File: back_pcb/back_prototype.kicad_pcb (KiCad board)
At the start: 2 copper layers, 40 x 100 mm, 358 parts

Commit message: Started new back PCB
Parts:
- removed ? (x330): , single_proto_pad:PROTO_PAD
- removed AB2_PERF_RAILS_1x1.7IN: VAL**, prototyping_area_10x14:PROTO_AREA_10x14
- removed W10: RXD, Measurement_Points:Measurement_Point_Square-SMD-Pad_Small
- removed W13: SDA, Measurement_Points:Measurement_Point_Square-SMD-Pad_Small
- removed W14: SCL, Measurement_Points:Measurement_Point_Square-SMD-Pad_Small
- removed W15: MOSI, Measurement_Points:Measurement_Point_Square-SMD-Pad_Small
- removed W16: MISO, Measurement_Points:Measurement_Point_Square-SMD-Pad_Small
- removed W17: SCK, Measurement_Points:Measurement_Point_Square-SMD-Pad_Small
- removed W18: , Measurement_Points:Measurement_Point_Square-SMD-Pad_Small
- removed W19: CS1, Measurement_Points:Measurement_Point_Square-SMD-Pad_Small
- removed W20: GP4, Measurement_Points:Measurement_Point_Square-SMD-Pad_Small
- removed W21: GP17, Measurement_Points:Measurement_Point_Square-SMD-Pad_Small
- removed W22: GP12, Measurement_Points:Measurement_Point_Square-SMD-Pad_Small
- removed W23: GP16, Measurement_Points:Measurement_Point_Square-SMD-Pad_Small
- removed W24: GP20, Measurement_Points:Measurement_Point_Square-SMD-Pad_Small
- removed W25: GP21, Measurement_Points:Measurement_Point_Square-SMD-Pad_Small
- removed W26, W6, W8: GND, Measurement_Points:Measurement_Point_Square-SMD-Pad_Small
- removed W9: TXD, Measurement_Points:Measurement_Point_Square-SMD-Pad_Small
- added C1: C_Small, Capacitors_SMD:C_0805, F.Cu at (63.8, 116.9)
- added C10: C_Small, Capacitors_SMD:C_0805, F.Cu at (74.8, 46.4)
- added C11: C_Small, Capacitors_SMD:C_0603, F.Cu at (78.5, 50.2)
- added C12: C, Capacitors_SMD:C_0603, F.Cu at (73.2, 50.2)
- added C13: C_Small, Capacitors_SMD:C_0805, B.Cu at (75.0, 62.6)
- added C14: C_Small, Capacitors_SMD:C_0805, F.Cu at (59.1, 121.8)
- added C15: C_Small, Capacitors_Tantalum_SMD:CP_Tantalum_Case-B_EIA-3528-21_Hand, B.Cu at (67.9, 84.3)
- added C16: C_Small, Capacitors_SMD:C_0603, F.Cu at (45.8, 58.4)
- added C17: C_Small, Capacitors_SMD:C_0603, F.Cu at (46.7, 56.7)
- added C18: C_Small, Capacitors_SMD:C_0603, F.Cu at (47.8, 58.5)
- added C19: C_Small, Capacitors_SMD:C_0603, F.Cu at (48.1, 47.5)
- added C2: C_Small, Capacitors_SMD:C_0805, B.Cu at (51.9, 119.1)
- added C20: C_Small, Capacitors_SMD:C_0603, F.Cu at (46.2, 48.2)
- added C21: C_Small, Capacitors_SMD:C_0603, F.Cu at (48.1, 48.9)
- added C22: C_Small, Capacitors_SMD:C_0603, F.Cu at (56.8, 131.8)
- added C23: C_Small, Capacitors_SMD:C_0603, F.Cu at (59.4, 131.8)
- added C24: C_Small, Capacitors_SMD:C_0603, F.Cu at (61.2, 131.0)
- added C25: C_Small, Capacitors_SMD:C_0805, B.Cu at (45.8, 64.1)
- added C3: C_Small, Capacitors_SMD:C_0805, B.Cu at (51.9, 114.7)
- added C4: C_Small, Capacitors_SMD:C_0805, F.Cu at (46.6, 119.0)
- added C5: C_Small, Capacitors_SMD:C_0805, B.Cu at (67.2, 118.9)
- added C6: C_Small, Capacitors_SMD:C_0805, B.Cu at (57.1, 66.8)
- added C7: C_Small, Capacitors_SMD:C_0805, B.Cu at (69.1, 120.1)
- added C8: C_Small, Capacitors_SMD:C_0805, F.Cu at (50.9, 65.0)
- added C9: C, Capacitors_SMD:C_0805, F.Cu at (77.6, 46.4)
- added D1: D, Diodes_SMD:MiniMELF_Handsoldering, B.Cu at (43.5, 63.9)
- added IC1: ATMEGA328P-A, Housings_QFP:TQFP-32_7x7mm_Pitch0.8mm, B.Cu at (60.9, 119.3)
- added JACK1: AB2_JACK_3.5MM-4P, footprints:4P_RPi_AV_jack, F.Cu at (75.9, 52.6)
- added JP1: JUMPER, Connect:GS2, B.Cu at (77.5, 62.2)
- added JP2: JUMPER, Connect:GS2, B.Cu at (72.5, 62.4)
- added P1: SwitchableHeader-3x08, switchable_header:Pin_Header_Straight_1x08, F.Cu at (53.3, 73.3)
- added P2: CONN_01X08, Pin_Headers:Pin_Header_Straight_1x08, F.Cu at (53.3, 47.0)
- added P3: CONN_01X04, Pin_Headers:Pin_Header_Straight_1x04_Pitch2.54mm, F.Cu at (77.5, 57.0)
- added P4: CONN_01X03, Pin_Headers:Pin_Header_Straight_1x03_Pitch2.54mm, F.Cu at (77.5, 67.2)
- added P5: CONN_01X04, Pin_Headers:Pin_Header_Straight_1x04_Pitch2.54mm, F.Cu at (44.5, 54.6)
- added P6: CONN_01X07, Pin_Headers:Pin_Header_Straight_1x07_Pitch2.54mm, F.Cu at (44.1, 128.3)
- added Q1: BC547, footprints:SOT-23_BC847B_Handsoldering, B.Cu at (45.7, 69.3)
- added Q2: BC547, footprints:SOT-23_BC847B_Handsoldering, B.Cu at (47.0, 83.4)
- added R1: R, Resistors_SMD:R_0603, B.Cu at (78.5, 54.4)
- added R10: R, Resistors_SMD:R_0805_HandSoldering, F.Cu at (65.4, 101.0)
- added R11: R, Resistors_SMD:R_0805_HandSoldering, B.Cu at (54.6, 131.5)
- added R12: R, Resistors_SMD:R_0805_HandSoldering, B.Cu at (45.1, 73.7)
- added R13: R, Resistors_SMD:R_0805_HandSoldering, B.Cu at (45.8, 79.2)
- added R14: R_Small, Resistors_SMD:R_0603, B.Cu at (77.0, 59.6)
- added R15: R_Small, Resistors_SMD:R_0603, B.Cu at (73.0, 59.6)
- added R16: R_Small, Resistors_SMD:R_0805, B.Cu at (45.8, 60.7)
- added R2: R_Small, Resistors_SMD:R_0603, B.Cu at (73.0, 54.4)
- added R3: R, Resistors_SMD:R_0805_HandSoldering, F.Cu at (69.0, 124.1)
- added R4: R, Resistors_SMD:R_0805_HandSoldering, F.Cu at (69.0, 122.1)
- added R5: R, Resistors_SMD:R_0805_HandSoldering, F.Cu at (65.4, 91.4)
- added R6: R, Resistors_SMD:R_0805_HandSoldering, F.Cu at (65.4, 93.3)
- added R7: R, Resistors_SMD:R_0805_HandSoldering, F.Cu at (65.4, 95.2)
- added R8: R, Resistors_SMD:R_0805_HandSoldering, F.Cu at (65.4, 97.2)
- added R9: R, Resistors_SMD:R_0805_HandSoldering, F.Cu at (65.4, 99.1)
- added U2: ESP-12E, ESP12E_SMD:ESP-12E_-1_-22, B.Cu at (49.5, 88.9)
- added U3: KEYPAD_OVERLAY, common-footprints:keypad_overlay, F.Cu at (41.5, 80.0)
- added X1: CRYSTAL_TH_SMD, footprints:Crystal_HC49_CSTCE, B.Cu at (53.8, 114.4)
- U1: value (none) -> Pi0Top; footprint Pi0Top:Pi0Top -> common-footprints:pi0outline
- W1: value 3V3 -> TEST_1P
- W11: value VBAT -> TEST_1P
- W12, W5, W7: value GND -> TEST_1P
- W2: value GP1 -> TEST_1P
- W3: value RST -> MIC; footprint Measurement_Points:Measurement_Point_Square-SMD-Pad_Small -> Terminal_Blocks:TerminalBlock_Pheonix_PT-3.5mm_2pol; moved to F.Cu
- W4: value TV_OUT -> TEST_1P
- moved W4 90.8 mm to (48.3, 44.8)
- moved W5 55.3 mm to (48.3, 42.7)
- moved U1 41.3 mm to (72.6, 83.3)
- moved W7 27.2 mm to (60.0, 109.0)
- moved W2 21.0 mm to (79.5, 95.4)
- moved W1 14.2 mm to (79.5, 93.0)
- moved W3 10.4 mm to (59.9, 136.4)
- moved W12 7.76 mm to (65.1, 126.7)
- moved W11 6.49 mm to (79.7, 79.7)
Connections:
- U1 pad 11: Net-(U1-Pad11) -> KEYPAD_GPIO
- U1 pad 12: Net-(U1-Pad12) -> AUDIO_0
- U1 pad 13: Net-(U1-Pad13) -> SD_D3
- U1 pad 15: Net-(U1-Pad15) -> SD_CLK
- U1 pad 16: Net-(U1-Pad16) -> SD_CMD
- U1 pad 18: Net-(U1-Pad18) -> SD_D0
- U1 pad 19: Net-(U1-Pad19) -> DI
- U1 pad 21: Net-(U1-Pad21) -> (no net)
- U1 pad 22: Net-(U1-Pad22) -> SD_D1
- U1 pad 23: Net-(U1-Pad23) -> SCK
- U1 pad 24: Net-(U1-Pad24) -> CS
- U1 pad 26: Net-(U1-Pad26) -> (no net)
- U1 pad 27: Net-(U1-Pad27) -> SD_RST
- U1 pad 28: Net-(U1-Pad28) -> (no net)
- U1 pad 29: Net-(U1-Pad29) -> DISPLAY_RST
- U1 pad 3: Net-(U1-Pad3) -> SDA
- U1 pad 31: Net-(U1-Pad31) -> DISPLAY_DC
- U1 pad 32: Net-(U1-Pad32) -> (no net)
- U1 pad 33: Net-(U1-Pad33) -> AUDIO_1
- U1 pad 35: Net-(U1-Pad35) -> (no net)
- U1 pad 36: Net-(U1-Pad36) -> (no net)
- U1 pad 37: Net-(U1-Pad37) -> SD_D2
- U1 pad 38: Net-(U1-Pad38) -> (no net)
- U1 pad 40: Net-(U1-Pad40) -> KEYPAD_INT
- U1 pad 41: Net-(U1-Pad41) -> (no net)
- U1 pad 42: Net-(U1-Pad42) -> (no net)
- U1 pad 43: Net-(U1-Pad43) -> (no net)
- U1 pad 44: GND -> (no net)
- U1 pad 5: Net-(U1-Pad5) -> SCL
- U1 pad 7: Net-(U1-Pad7) -> (no net)
- W1 pad 1: +3V3 -> Net-(U1-Pad8)
- W2 pad 1: Net-(U1-Pad28) -> Net-(U1-Pad10)
- W3 pad 1: Net-(U1-Pad42) -> Net-(C16-Pad2)
- W4 pad 1: Net-(U1-Pad43) -> Net-(C20-Pad2)
- W5 pad 1: GND -> Net-(C19-Pad2)
- W7 pad 1: GND -> VIBRO_PWM
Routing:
- net GND: track 73.1 -> 550.0 mm, vias 0 -> 167
- net +3V3: track 5.08 -> 192.4 mm, vias 0 -> 11
- net Net-(C17-Pad2): track 0.00 -> 99.0 mm, vias 0 -> 1
- net Net-(C16-Pad2): track 0.00 -> 93.3 mm, vias 0 -> 1
- net DISPLAY_RST: track 0.00 -> 79.2 mm, vias 0 -> 3
- net DISPLAY_DC: track 0.00 -> 73.6 mm, vias 0 -> 3
- net SDA: track 0.00 -> 67.1 mm, vias 0 -> 3
- net AUDIO_1: track 0.00 -> 65.8 mm, vias 0 -> 1
- net VPP: track 5.08 -> 70.7 mm, vias 0 -> 2
- net SCL: track 0.00 -> 64.9 mm, vias 0 -> 3
- net CS: track 0.00 -> 64.2 mm, vias 0 -> 1
- net VIBRO_PWM: track 0.00 -> 54.4 mm, vias 0 -> 3
- net SCK: track 0.00 -> 47.2 mm, vias 0 -> 1
- net DI: track 0.00 -> 46.8 mm, vias 0 -> 1
- net DISPLAY_BL: track 0.00 -> 43.7 mm
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- added copper zone on B.Cu, net GND
- added copper zone on F.Cu, net GND
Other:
- outline, holes or cut-outs redrawn
- net class Default: clearance 0.2 -> 0.16
- rule trace_clearance: 0.2 -> 0.16
- rule via_min_drill: 0.3 -> 0.25
- board text removed: "Designed in MakeRiga"
- board text removed: "Made with KiCad"
- board text removed: "Merry Christmas!"
- board text removed: "ProtoZero Christmas"

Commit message: Back board almost finished
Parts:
- removed C1, C10, C2, C3: C_Small, Capacitors_SMD:C_0805
- removed C11: C_Small, Capacitors_SMD:C_0603
- removed C12: C, Capacitors_SMD:C_0603
- removed C9: C, Capacitors_SMD:C_0805
- removed IC1: ATMEGA328P-A, Housings_QFP:TQFP-32_7x7mm_Pitch0.8mm
- removed JACK1: AB2_JACK_3.5MM-4P, footprints:4P_RPi_AV_jack
- removed R10, R11, R12, R13: R, Resistors_SMD:R_0805_HandSoldering
- removed R14, R15: R_Small, Resistors_SMD:R_0603
- removed R16: R_Small, Resistors_SMD:R_0805
- removed X1: CRYSTAL_TH_SMD, footprints:Crystal_HC49_CSTCE
- added JP10: Jumper_NC_Small, Connect:GS2, B.Cu at (56.9, 87.2)
- added JP3: JUMPER3, Connect:GS3, B.Cu at (47.3, 67.9)
- added JP4: JUMPER3, Connect:GS3, B.Cu at (51.4, 67.9)
- added JP5: JUMPER, Connect:GS2, F.Cu at (72.2, 64.5)
- added JP6: JUMPER3, Connect:GS3, B.Cu at (49.4, 67.9)
- added JP7: JUMPER3, Connect:GS3, B.Cu at (48.7, 82.6)
- added JP8: JUMPER3, Connect:GS3, B.Cu at (67.1, 44.8)
- added JP9: Jumper_NC_Small, Connect:GS2, B.Cu at (56.9, 92.7)
- added P7: EXPANSION_BOTTOM2, Pin_Headers:Pin_Header_Angled_1x02_Pitch2.54mm, B.Cu at (45.8, 130.0)
- added P8: CONN_01X02, footprints:JST_PH_S2B-PH-SM4-TB_02x2.00mm_Angled, F.Cu at (77.1, 68.3)
- added Q3: Q_NMOS_GSD, TO_SOT_Packages_SMD:SOT-23_Handsoldering, B.Cu at (58.2, 89.0)
- added U4: TP4056_BREAKOUT, footprints:TP4056_BREAKOUT, F.Cu at (54.5, 68.1)
- added U5: RTC, Housings_SOIC:SOIC-8_3.9x4.9mm_Pitch1.27mm, B.Cu at (46.8, 90.5)
- added W10: TEST_1P, Measurement_Points:Measurement_Point_Square-SMD-Pad_Small, B.Cu at (46.6, 123.2)
- added W13: TEST_1P, Measurement_Points:Measurement_Point_Square-SMD-Pad_Small, B.Cu at (46.6, 125.7)
- added W14: TEST_1P, Measurement_Points:Measurement_Point_Square-SMD-Pad_Small, B.Cu at (52.8, 45.1)
- added W15: BAT-, Measurement_Points:Measurement_Point_Square-SMD-Pad_Small, F.Cu at (96.4, 62.4)
- added W16: BAT+, Measurement_Points:Measurement_Point_Square-SMD-Pad_Small, B.Cu at (49.7, 45.1)
- added W17: TEST_1P, Measurement_Points:Measurement_Point_Square-SMD-Pad_Small, B.Cu at (37.6, 59.0)
- added W18: TEST_1P, Measurement_Points:Measurement_Point_Square-SMD-Pad_Small, B.Cu at (34.7, 66.4)
- added W19: TEST_1P, Measurement_Points:Measurement_Point_Square-SMD-Pad_Small, B.Cu at (29.9, 65.8)
- added W20: TEST_1P, Measurement_Points:Measurement_Point_Square-SMD-Pad_Small, B.Cu at (32.6, 73.4)
- added W21: TEST_1P, Measurement_Points:Measurement_Point_Square-SMD-Pad_Small, B.Cu at (31.7, 63.4)
- added W22: TEST_1P, Measurement_Points:Measurement_Point_Square-SMD-Pad_Small, B.Cu at (34.4, 57.8)
- added W23: TEST_1P, Measurement_Points:Measurement_Point_Square-SMD-Pad_Small, B.Cu at (29.0, 60.6)
- added W24: TEST_1P, Measurement_Points:Measurement_Point_Square-SMD-Pad_Small, B.Cu at (35.3, 61.3)
- added W25: TEST_1P, Measurement_Points:Measurement_Point_Square-SMD-Pad_Small, B.Cu at (53.8, 114.8)
- added W26: TEST_1P, Measurement_Points:Measurement_Point_Square-SMD-Pad_Small, B.Cu at (53.8, 117.9)
- added W27: TEST_1P, Measurement_Points:Measurement_Point_Square-SMD-Pad_Small, B.Cu at (46.6, 113.0)
- added W28: TEST_1P, Measurement_Points:Measurement_Point_Square-SMD-Pad_Small, B.Cu at (33.3, 69.2)
- added W29: TEST_1P, Measurement_Points:Measurement_Point_Square-SMD-Pad_Small, B.Cu at (46.6, 118.2)
- added W6: TEST_1P, Measurement_Points:Measurement_Point_Square-SMD-Pad_Small, B.Cu at (79.2, 88.4)
- added W8: TEST_1P, Measurement_Points:Measurement_Point_Square-SMD-Pad_Small, B.Cu at (46.6, 115.6)
- added W9: TEST_1P, Measurement_Points:Measurement_Point_Square-SMD-Pad_Small, B.Cu at (46.6, 120.7)
- added Y1: Crystal_Small, Crystals:Crystal_SMD_G8-2pin_3.2x1.5mm_HandSoldering, B.Cu at (47.9, 97.0)
- C15: footprint Capacitors_Tantalum_SMD:CP_Tantalum_Case-B_EIA-3528-21_Hand -> Capacitors_SMD:C_0805
- C16, C17, C18, C19, C20, C21, C22, C23, C24, R3, R4, R5, R6, R7, R8, R9: moved to B.Cu
- D1: value D -> D_Small; footprint Diodes_SMD:MiniMELF_Handsoldering -> Diodes_SMD:D_MiniMELF_Handsoldering
- P1: value SwitchableHeader-3x08 -> EXPANSION_LEFT; footprint switchable_header:Pin_Header_Straight_1x08 -> Pin_Headers:Pin_Header_Angled_1x13_Pitch2.54mm
- P2: value CONN_01X08 -> EXPANSION_BOTTOM; footprint Pin_Headers:Pin_Header_Straight_1x08 -> Pin_Headers:Pin_Header_Angled_1x04_Pitch2.54mm; moved to B.Cu
- P3: value CONN_01X04 -> EXPANSION_TOP; footprint Pin_Headers:Pin_Header_Straight_1x04_Pitch2.54mm -> Pin_Headers:Pin_Header_Angled_1x05_Pitch2.54mm; moved to B.Cu
- P4: value CONN_01X03 -> USB_A; footprint Pin_Headers:Pin_Header_Straight_1x03_Pitch2.54mm -> Connect:USB_A; moved to B.Cu
- P6: value CONN_01X07 -> ATMEGA_HEADER
- Q1: value BC547 -> Q_PMOS_GSD; footprint footprints:SOT-23_BC847B_Handsoldering -> TO_SOT_Packages_SMD:SOT-23_Handsoldering
- Q2: value BC547 -> Q_NMOS_GSD; footprint footprints:SOT-23_BC847B_Handsoldering -> TO_SOT_Packages_SMD:SOT-23_Handsoldering
- R1: footprint Resistors_SMD:R_0603 -> Resistors_SMD:R_0805_HandSoldering; moved to F.Cu
- R2: value R_Small -> R; footprint Resistors_SMD:R_0603 -> Resistors_SMD:R_0805_HandSoldering; moved to F.Cu
- U1: value Pi0Top -> PI ZERO
- U2: value ESP-12E -> SIM800_BREAKOUT; footprint ESP12E_SMD:ESP-12E_-1_-22 -> footprints:SIM800_BREAKOUT; moved to F.Cu
- U3: value KEYPAD_OVERLAY -> MCP23017; footprint common-footprints:keypad_overlay -> SMD_Packages:SOIC-28
- W11: value TEST_1P -> BAT_IN
- W3: value MIC -> TEST_1P; footprint Terminal_Blocks:TerminalBlock_Pheonix_PT-3.5mm_2pol -> Measurement_Points:Measurement_Point_Square-SMD-Pad_Small; moved to B.Cu
- W5: moved to F.Cu
- moved W4 93.3 mm to (67.6, 136.1)
- moved C4 90.1 mm to (108.3, 53.3)
- moved C14 87.4 mm to (116.6, 56.0)
- moved P2 83.1 mm to (56.0, 130.0), turned to 270 degrees
- moved W12 81.3 mm to (110.2, 59.1)
- moved C7 81.0 mm to (114.3, 53.0)
- moved C5 78.9 mm to (110.7, 53.1)
- moved C24 77.9 mm to (51.7, 53.7)
- moved C23 76.0 mm to (51.7, 56.2), turned to 90 degrees
- moved C22 73.2 mm to (51.7, 58.7), turned to 90 degrees
- moved C25 69.2 mm to (57.3, 132.4), turned to 0 degrees
- moved P4 61.7 mm to (58.6, 126.0), turned to 0 degrees
- moved R4 56.9 mm to (90.4, 69.3), turned to 270 degrees
- moved R3 46.8 mm to (63.1, 77.6), turned to 90 degrees
- moved C8 39.9 mm to (90.7, 61.9)
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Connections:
- C16 pad 2: Net-(C16-Pad2) -> MIC+
- C17 pad 1: Net-(C16-Pad2) -> MIC+
- C17 pad 2: Net-(C17-Pad2) -> MIC-
- C18 pad 1: Net-(C17-Pad2) -> MIC-
- C19 pad 2: Net-(C19-Pad2) -> SPK+
- C20 pad 1: Net-(C19-Pad2) -> SPK+
- C20 pad 2: Net-(C20-Pad2) -> SPK-
- C21 pad 1: Net-(C20-Pad2) -> SPK-
- C22 pad 2: Net-(C16-Pad2) -> MIC+
- C23 pad 1: Net-(C16-Pad2) -> MIC+
- C23 pad 2: Net-(C17-Pad2) -> MIC-
- C24 pad 1: Net-(C17-Pad2) -> MIC-
- D1 pad 1: Net-(D1-Pad1) -> VPP
- D1 pad 2: Net-(D1-Pad2) -> VDD
- JP1 pad 1: Net-(JP1-Pad1) -> +BATT
- JP1 pad 2: AUDIO_1 -> +BATT
- JP2 pad 1: AUDIO_0 -> RTC_ALARM
- P1 pad 1: DISPLAY_BL -> +BATT
- P1 pad 10: SCK -> MISO
- P1 pad 11: Net-(P1-Pad11) -> MOSI
- P1 pad 12: (no net) -> GND
- P1 pad 13: DI -> +3V3
- P1 pad 2: Net-(P1-Pad2) -> +5V
- P1 pad 3: GND -> TV_OUT
- P1 pad 4: +3V3 -> GND
- P1 pad 5: Net-(P1-Pad5) -> VDD
- P1 pad 6: GND -> LH_GPIO_2
- P1 pad 7: +3V3 -> LH_GPIO_1
- P1 pad 8: Net-(P1-Pad8) -> CS
- P1 pad 9: GND -> SCK
- P2 pad 1: Net-(P1-Pad2) -> +3V3
- P2 pad 2: Net-(P1-Pad5) -> GND
- P2 pad 3: Net-(P1-Pad8) -> SDA
- P2 pad 4: Net-(P1-Pad11) -> SCL
- P3 pad 1: Net-(JP1-Pad1) -> +5V
- P3 pad 2: GND -> +3V3
- P3 pad 3: Net-(JP2-Pad2) -> IR_TX
- P3 pad 4: MIC -> IR_RX
- P4 pad 1: AUDIO_1 -> +5V
- P4 pad 2: +3V3 -> USB_D-
- P4 pad 3: AUDIO_0 -> USB_D+
- P5 pad 1: Net-(C16-Pad2) -> MIC+
- P5 pad 2: Net-(C17-Pad2) -> MIC-
- P5 pad 3: Net-(C20-Pad2) -> SPK-
- P5 pad 4: Net-(C19-Pad2) -> SPK+
- P6 pad 7: +3V3 -> Net-(P6-Pad7)
- Q1 pad 1: Net-(D1-Pad2) -> VDD
- Q1 pad 2: Net-(Q1-Pad2) -> VPP
- Q1 pad 3: GND -> +BATT
- Q2 pad 1: KEYPAD_BL- -> GND
- Q2 pad 2: Net-(Q2-Pad2) -> SCL
- Q2 pad 3: GND -> Net-(JP9-Pad1)
- R1 pad 1: Net-(C11-Pad1) -> VDD
- R1 pad 2: GND -> CHARGING_SENSE
- R2 pad 1: GND -> CHARGING_SENSE
- R2 pad 2: Net-(C10-Pad2) -> GND
- R3 pad 1: Net-(IC1-Pad22) -> VDD
- R3 pad 2: VPP -> GND
- R4 pad 1: Net-(IC1-Pad22) -> (no net)
- R4 pad 2: GND -> FLASH_LED
- R5 pad 1: SD_CMD -> (no net)
- R5 pad 2: Net-(R5-Pad2) -> NOTIF_LED_R
- R6 pad 1: SD_D0 -> (no net)
- R6 pad 2: Net-(R6-Pad2) -> NOTIF_LED_G
- R7 pad 1: SD_D2 -> (no net)
- R7 pad 2: Net-(R7-Pad2) -> NOTIF_LED_B
- R8 pad 1: SD_D3 -> +3V3
- R8 pad 2: Net-(R8-Pad2) -> Net-(JP9-Pad1)
- R9 pad 1: SD_D1 -> Net-(JP10-Pad1)
- R9 pad 2: Net-(R9-Pad2) -> +3V3
- U1 pad 10: Net-(U1-Pad10) -> SIM800_TXD
- U1 pad 11: KEYPAD_GPIO -> (no net)
- U1 pad 12: AUDIO_0 -> (no net)
- U1 pad 13: SD_D3 -> (no net)
- U1 pad 15: SD_CLK -> (no net)
- U1 pad 16: SD_CMD -> (no net)
- U1 pad 18: SD_D0 -> (no net)
- U1 pad 19: DI -> MOSI
- U1 pad 21: (no net) -> MISO
- U1 pad 22: SD_D1 -> (no net)
- U1 pad 24: CS -> (no net)
- U1 pad 26: (no net) -> CS
- U1 pad 27: SD_RST -> (no net)
- U1 pad 28: (no net) -> MCP_INT
- U1 pad 29: DISPLAY_RST -> (no net)
- U1 pad 31: DISPLAY_DC -> (no net)
- U1 pad 32: (no net) -> IR_RX
- U1 pad 33: AUDIO_1 -> (no net)
- U1 pad 35: (no net) -> LH_GPIO_1
- U1 pad 36: (no net) -> LH_GPIO_2
- U1 pad 37: SD_D2 -> (no net)
- U1 pad 38: (no net) -> BH_GPIO
- U1 pad 40: KEYPAD_INT -> (no net)
- U1 pad 42: (no net) -> PI_RST
- U1 pad 43: (no net) -> TV_OUT
- U1 pad 44: (no net) -> Net-(U1-Pad44)
- U1 pad 7: (no net) -> IR_TX
- U1 pad 8: Net-(U1-Pad8) -> SIM800_RXD
- U2 pad 10: Net-(R6-Pad2) -> SPK+
- U2 pad 11: Net-(R7-Pad2) -> SPK-
- U2 pad 2: (no net) -> SIM800_RST
- U2 pad 3: SD_RST -> SIM800_RXD
- U2 pad 4: (no net) -> SIM800_TXD
- U2 pad 5: (no net) -> GND
- U2 pad 6: (no net) -> SIM800_RING
- U2 pad 7: (no net) -> SIM800_DTR
- U2 pad 8: +3V3 -> MIC+
- U2 pad 9: Net-(R5-Pad2) -> MIC-
- U3 pad 1: ROW5 -> SIM800_DTR
- U3 pad 10: COL5 -> GND
- U3 pad 11: COL6 -> (no net)
- U3 pad 12: +3V3 -> SCL
- U3 pad 13: KEYPAD_BL- -> SDA
- U3 pad 14: +3V3 -> (no net)
- U3 pad 15: SDA -> GND
- U3 pad 16: SCL -> GND
- U3 pad 18: KEYPAD_GPIO -> (no net)
- U3 pad 2: ROW4 -> SIM800_RING
- U3 pad 3: ROW3 -> SIM800_RST
- U3 pad 4: ROW2 -> (no net)
- U3 pad 5: ROW1 -> (no net)
- U3 pad 6: COL1 -> (no net)
- U3 pad 7: COL2 -> Net-(JP2-Pad2)
- U3 pad 8: COL3 -> CHARGING_SENSE
- U3 pad 9: COL4 -> +3V3
- W1 pad 1: Net-(U1-Pad8) -> SIM800_RXD
- W11 pad 1: VPP -> +BATT
- W2 pad 1: Net-(U1-Pad10) -> SIM800_TXD
- W3 pad 1: Net-(C16-Pad2) -> PI_RST
- W4 pad 1: Net-(C20-Pad2) -> Net-(U1-Pad44)
- W5 pad 1: Net-(C19-Pad2) -> GND
- W7 pad 1: VIBRO_PWM -> IR_RX
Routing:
- net GND: track 550.0 -> 30.0 mm, vias 167 -> 3
- net +BATT: track 0.00 -> 112.5 mm
- net Net-(C17-Pad2): track 99.0 -> 0.00 mm, vias 1 -> 0
- net Net-(C16-Pad2): track 93.3 -> 0.00 mm, vias 1 -> 0
- net IR_RX: track 0.00 -> 82.7 mm, vias 0 -> 1
- net DISPLAY_RST: track 79.2 -> 0.00 mm, vias 3 -> 0
- net DISPLAY_DC: track 73.6 -> 0.00 mm, vias 3 -> 0
- net AUDIO_1: track 65.8 -> 0.00 mm, vias 1 -> 0
- net VPP: track 70.7 -> 9.19 mm, vias 2 -> 0
- net +3V3: track 192.4 -> 132.4 mm, vias 11 -> 1
- net IR_TX: track 0.00 -> 56.9 mm, vias 0 -> 1
- net VIBRO_PWM: track 54.4 -> 0.00 mm, vias 3 -> 0
- net LH_GPIO_2: track 0.00 -> 50.4 mm
- net MCP_INT: track 0.00 -> 49.5 mm, vias 0 -> 2
- net LH_GPIO_1: track 0.00 -> 48.8 mm
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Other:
- outline, holes or cut-outs redrawn

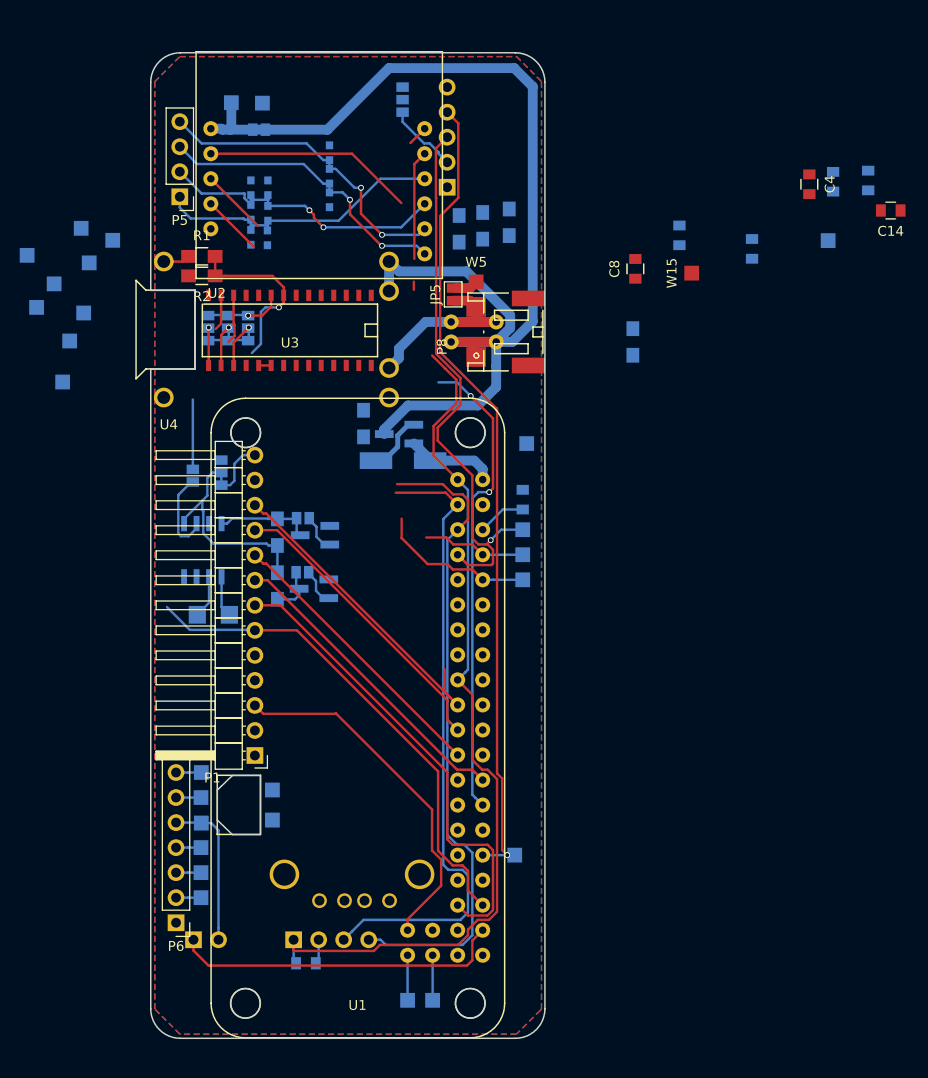
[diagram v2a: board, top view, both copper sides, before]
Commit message: Back board finished - untested, not pretty
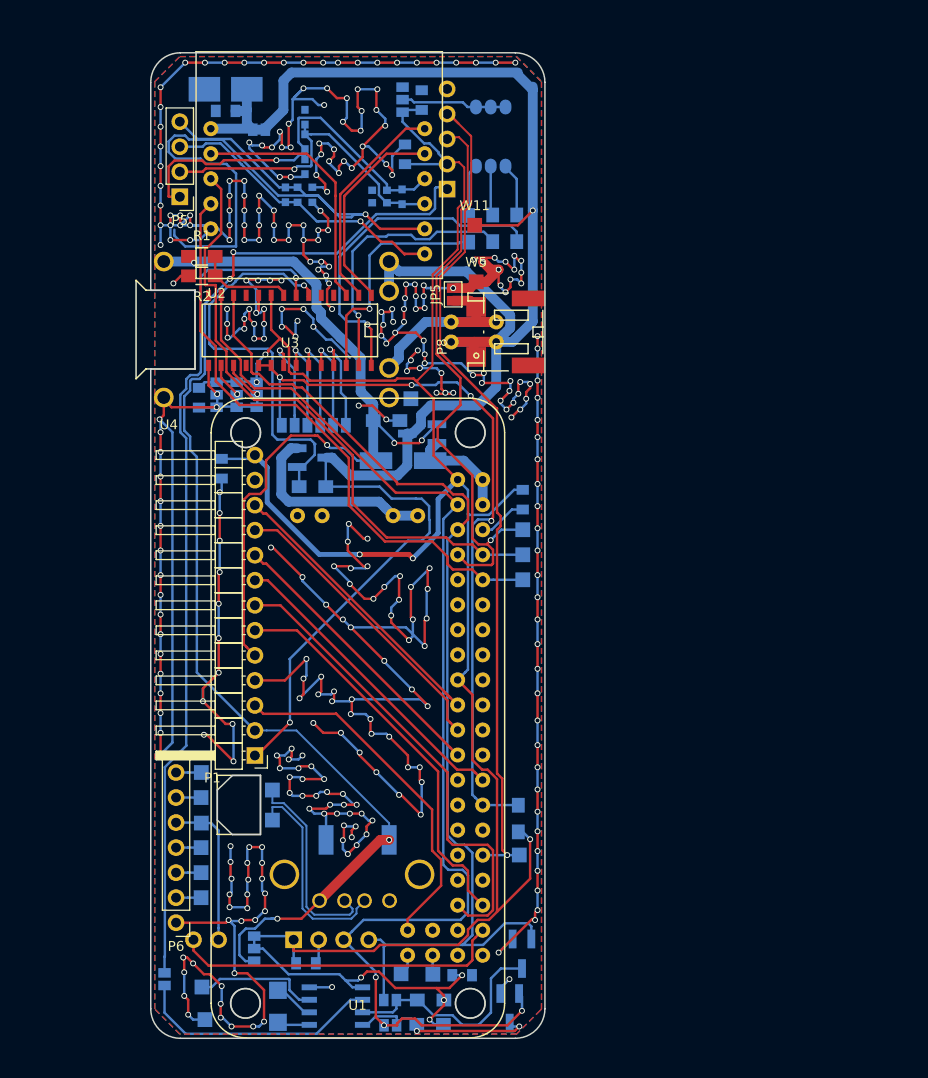
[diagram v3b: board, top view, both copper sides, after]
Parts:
- removed R4: R, Resistors_SMD:R_0805_HandSoldering
- removed W17, W18, W19, W20: TEST_1P, Measurement_Points:Measurement_Point_Square-SMD-Pad_Small
- added D3: Led_RGB_CA, footprints:RGB_5050, B.Cu at (76.0, 48.5)
- added Q4: Q_PMOS_GSD, TO_SOT_Packages_SMD:SOT-23_Handsoldering, B.Cu at (57.9, 81.1)
- added R10: R, Resistors_SMD:R_0805_HandSoldering, B.Cu at (57.9, 84.0)
- added R11: R, Resistors_SMD:R_0805_HandSoldering, B.Cu at (78.8, 117.7)
- added U6: DC_DC_BREAKOUT, footprints:DC-DC-BREAKOUT, B.Cu at (62.5, 101.9)
- C14, C8: moved to B.Cu
- C4: footprint Capacitors_SMD:C_0805 -> Capacitors_Tantalum_SMD:CP_Tantalum_Case-B_EIA-3528-21_Hand; moved to B.Cu
- W11: moved to F.Cu
- W15: value BAT- -> RTC_BAT; moved to B.Cu
- W16: value BAT+ -> TEST_1P
- moved W14 93.2 mm to (47.0, 138.1)
- moved C7 90.6 mm to (73.1, 133.6), turned to 0 degrees
- moved W15 87.8 mm to (46.7, 134.8), turned to 0 degrees
- moved C14 72.7 mm to (46.4, 75.0), turned to 270 degrees
- moved C5 62.1 mm to (49.1, 45.9), turned to 180 degrees
- moved C4 60.0 mm to (49.1, 43.7), turned to 180 degrees
- moved R9 52.3 mm to (69.8, 138.6), turned to 0 degrees
- moved JP10 52.2 mm to (65.8, 138.7), turned to 90 degrees
- moved Q3 51.9 mm to (77.9, 137.0), turned to 270 degrees
- moved JP2 51.2 mm to (42.9, 134.0)
- moved JP7 48.4 mm to (52.0, 130.9), turned to 180 degrees
- moved U5 48.2 mm to (60.3, 136.7), turned to 0 degrees
- moved C8 46.6 mm to (48.7, 82.2), turned to 270 degrees
- moved W12 45.3 mm to (67.9, 75.1)
- moved R8 44.8 mm to (69.9, 136.1), turned to 180 degrees
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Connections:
- C4 pad 1: +3V3 -> +BATT
- C5 pad 1: +3V3 -> +BATT
- JP8 pad 2: (no net) -> Net-(D3-Pad1)
- R5 pad 1: (no net) -> Net-(D3-Pad2)
- R6 pad 1: (no net) -> Net-(D3-Pad3)
- R7 pad 1: (no net) -> Net-(D3-Pad4)
- U3 pad 25: FLASH_LED -> Net-(U3-Pad25)
- U3 pad 6: (no net) -> DCDC_EN
- U5 pad 3: (no net) -> Net-(U5-Pad3)
- W15 pad 1: BATT- -> Net-(U5-Pad3)
- W16 pad 1: +BATT -> Net-(U3-Pad25)
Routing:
- net GND: track 30.0 -> 778.0 mm, vias 3 -> 346
- net +5V: track 0.00 -> 122.6 mm, vias 0 -> 4
- net +3V3: track 132.4 -> 249.1 mm, vias 1 -> 9
- net Net-(JP2-Pad2): track 7.08 -> 85.4 mm, vias 0 -> 1
- net VDD: track 8.77 -> 83.2 mm, vias 0 -> 4
- net +BATT: track 112.5 -> 184.0 mm, vias 0 -> 2
- net SDA: track 71.9 -> 121.5 mm, vias 0 -> 3
- net SIM800_RXD: track 17.3 -> 63.0 mm
- net SPK+: track 31.9 -> 76.9 mm, vias 2 -> 1
- net DCDC_EN: track 0.00 -> 42.0 mm, vias 0 -> 1
- net SIM800_TXD: track 22.2 -> 61.8 mm
- net NOTIF_LED_R: track 0.00 -> 34.6 mm, vias 0 -> 1
- net SCL: track 74.4 -> 108.6 mm
- net NOTIF_LED_G: track 0.00 -> 27.7 mm, vias 0 -> 1
- net MCP_INT: track 49.5 -> 76.6 mm, vias 2 -> 4
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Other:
- net class Default: clearance 0.16 -> 0.15; trace_width 0.25 -> 0.1
- rule trace_clearance: 0.16 -> 0.15
- rule trace_min: 0.2 -> 0.1

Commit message: OpenGL router fuckup
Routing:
- net SPK+: track 76.9 -> 29.9 mm
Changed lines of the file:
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@@
     (thickness 1.6)
     (drawings 22)
-    (tracks 1845)
+    (tracks 1827)
     (zones 0)
     (modules 84)
@@
   )
   (setup
-    (last_trace_width 0.25)
+    (last_trace_width 0.1)
     (user_trace_width 0.2)
     (user_trace_width 0.25)
@@
     (fp_line (start 1 -1) (end -1 -1) (layer B.CrtYd) (width 0.05))
     (fp_line (start -1 -1) (end -1 1) (layer B.CrtYd) (width 0.05))
-    (pad 1 smd rect (at 0 1.5 360) (size 1 1.5) (layers B.Cu B.Mask)
+    (pad 1 smd rect (at 0 1.5) (size 1 1.5) (layers B.Cu B.Mask)
       (net 52 "Net-(U3-Pad23)"))
   )
@@
   (segment (start 66.8648 55.2196) (end 67.0052 55.36) (width 0.25) (layer B.Cu) (net 15))
   (segment (start 57.15 48.247) (end 57.15 48.272) (width 0.25) (layer B.Cu) (net 15))
-  (segment (start 60.389202 56.388) (end 58.483001 54.481799) (width 0.25) (layer B.Cu) (net 16))
-  (segment (start 44.996801 59.645799) (end 43.90001 58.549008) (width 0.25) (layer B.Cu) (net 16))
-  (segment (start 43.909999 48.404999) (end 43.324999 48.989999) (width 0.25) (layer B.Cu) (net 16))
-  (segment (start 63.2968 56.388) (end 60.389202 56.388) (width 0.25) (layer B.Cu) (net 16))
-  (segment (start 58.483001 54.481799) (end 54.434498 54.481799) (width 0.25) (layer B.Cu) (net 16))
-  (segment (start 54.434498 54.481799) (end 48.746888 48.794189) (width 0.25) (layer B.Cu) (net 16))
-  (segment (start 47.101839 51.278201) (end 49.175841 51.278201) (width 0.25) (layer B.Cu) (net 16))
-  (segment (start 48.746888 48.794189) (end 45.379191 48.794189) (width 0.25) (layer B.Cu) (net 16))
-  (segment (start 49.175841 51.278201) (end 50.161601 52.263961) (width 0.25) (layer B.Cu) (net 16))
-  (segment (start 45.379191 48.794189) (end 44.990001 48.404999) (width 0.25) (layer B.Cu) (net 16))
-  (segment (start 46.562599 50.738961) (end 47.101839 51.278201) (width 0.25) (layer B.Cu) (net 16))
-  (segment (start 44.990001 48.404999) (end 43.909999 48.404999) (width 0.25) (layer B.Cu) (net 16))
-  (segment (start 50.161601 52.263961) (end 50.161601 59.645799) (width 0.25) (layer B.Cu) (net 16))
-  (segment (start 43.324999 48.989999) (end 43.324999 50.070001) (width 0.25) (layer B.Cu) (net 16))
-  (segment (start 43.324999 50.070001) (end 43.993959 50.738961) (width 0.25) (layer B.Cu) (net 16))
-  (segment (start 50.161601 59.645799) (end 44.996801 59.645799) (width 0.25) (layer B.Cu) (net 16))
-  (segment (start 43.993959 50.738961) (end 46.562599 50.738961) (width 0.25) (layer B.Cu) (net 16))
-  (segment (start 43.90001 58.549008) (end 43.90001 57.950992) (width 0.25) (layer B.Cu) (net 16))
   (segment (start 63.2968 56.388) (end 64.77 57.8612) (width 0.25) (layer F.Cu) (net 16))
   (segment (start 64.77 57.8612) (end 69.2996 57.8612) (width 0.25) (layer F.Cu) (net 16))

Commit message: Added component values to the back PCB - for BOM
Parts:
- C13, C14, C15, C25, C5, C6, C7, C8: value C_Small -> 100nF
- C16, C17, C18, C19, C20, C21: value C_Small -> 10pF
- C22, C23, C24: value C_Small -> 33pF
- C4: value C_Small -> 10uF
- D1: value D_Small -> SS14
- D3: value Led_RGB_CA -> Led_RGB_CA_CC
- JP3: value JUMPER3 -> A0
- JP4: value JUMPER3 -> A1
- JP6: value JUMPER3 -> A2
- JP7: value JUMPER3 -> 3V3/5V
- JP8: value JUMPER3 -> CA/CC
- P5: value CONN_01X04 -> AUDIO_CONN
- Q1, Q4: value Q_PMOS_GSD -> IRLML6401
- Q2, Q3: value Q_NMOS_GSD -> BSS138
- R1, R10, R11, R2, R3, R8, R9: value R -> 10K
- R5, R6, R7: value R -> 1K
- Y1: value Crystal_Small -> 32.768Hz
